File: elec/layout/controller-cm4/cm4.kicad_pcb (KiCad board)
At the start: 2 copper layers, 15 parts, among them U10 12.4kΩ ±1% 62.5mW, U13 1MΩ ±1% 62.5mW, U32 49.9Ω ±1% 62.5mW, U37 10kΩ ±1% 62.5mW

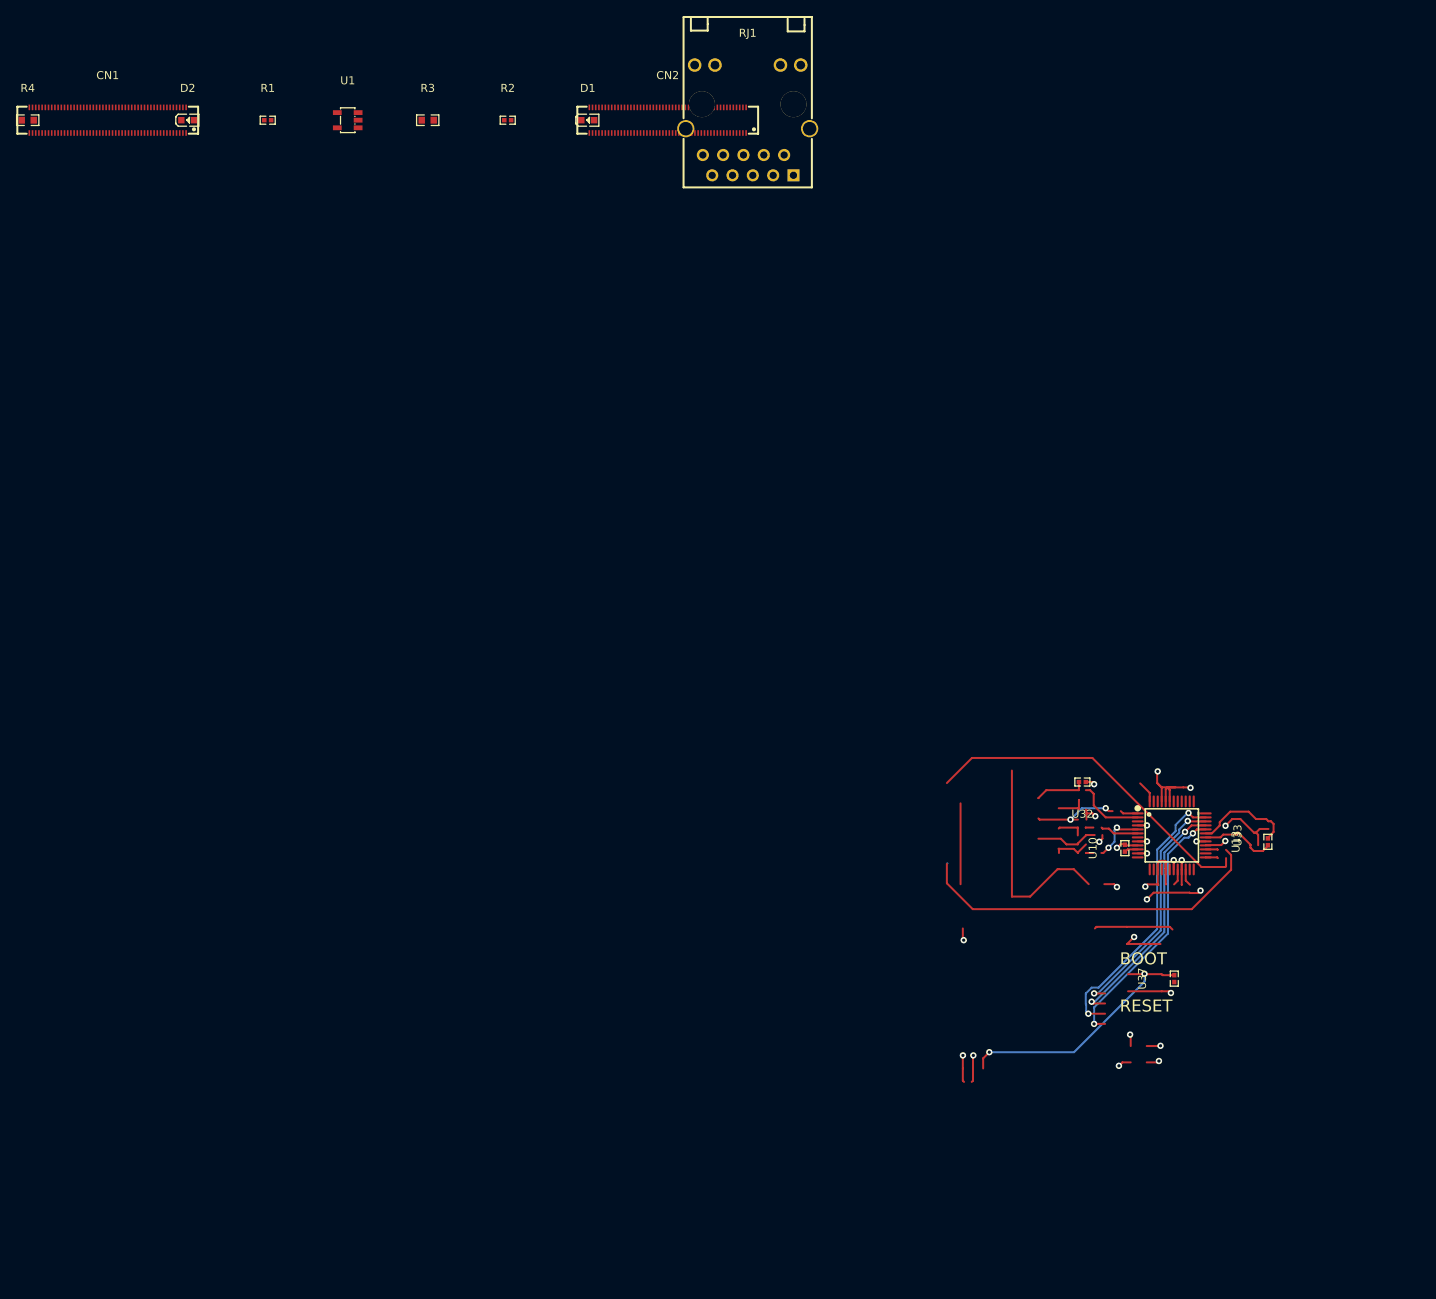
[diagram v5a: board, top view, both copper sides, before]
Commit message: Fix layout for CM4, update ato, delete CM4 example, replacing with SpaceBMSHIL
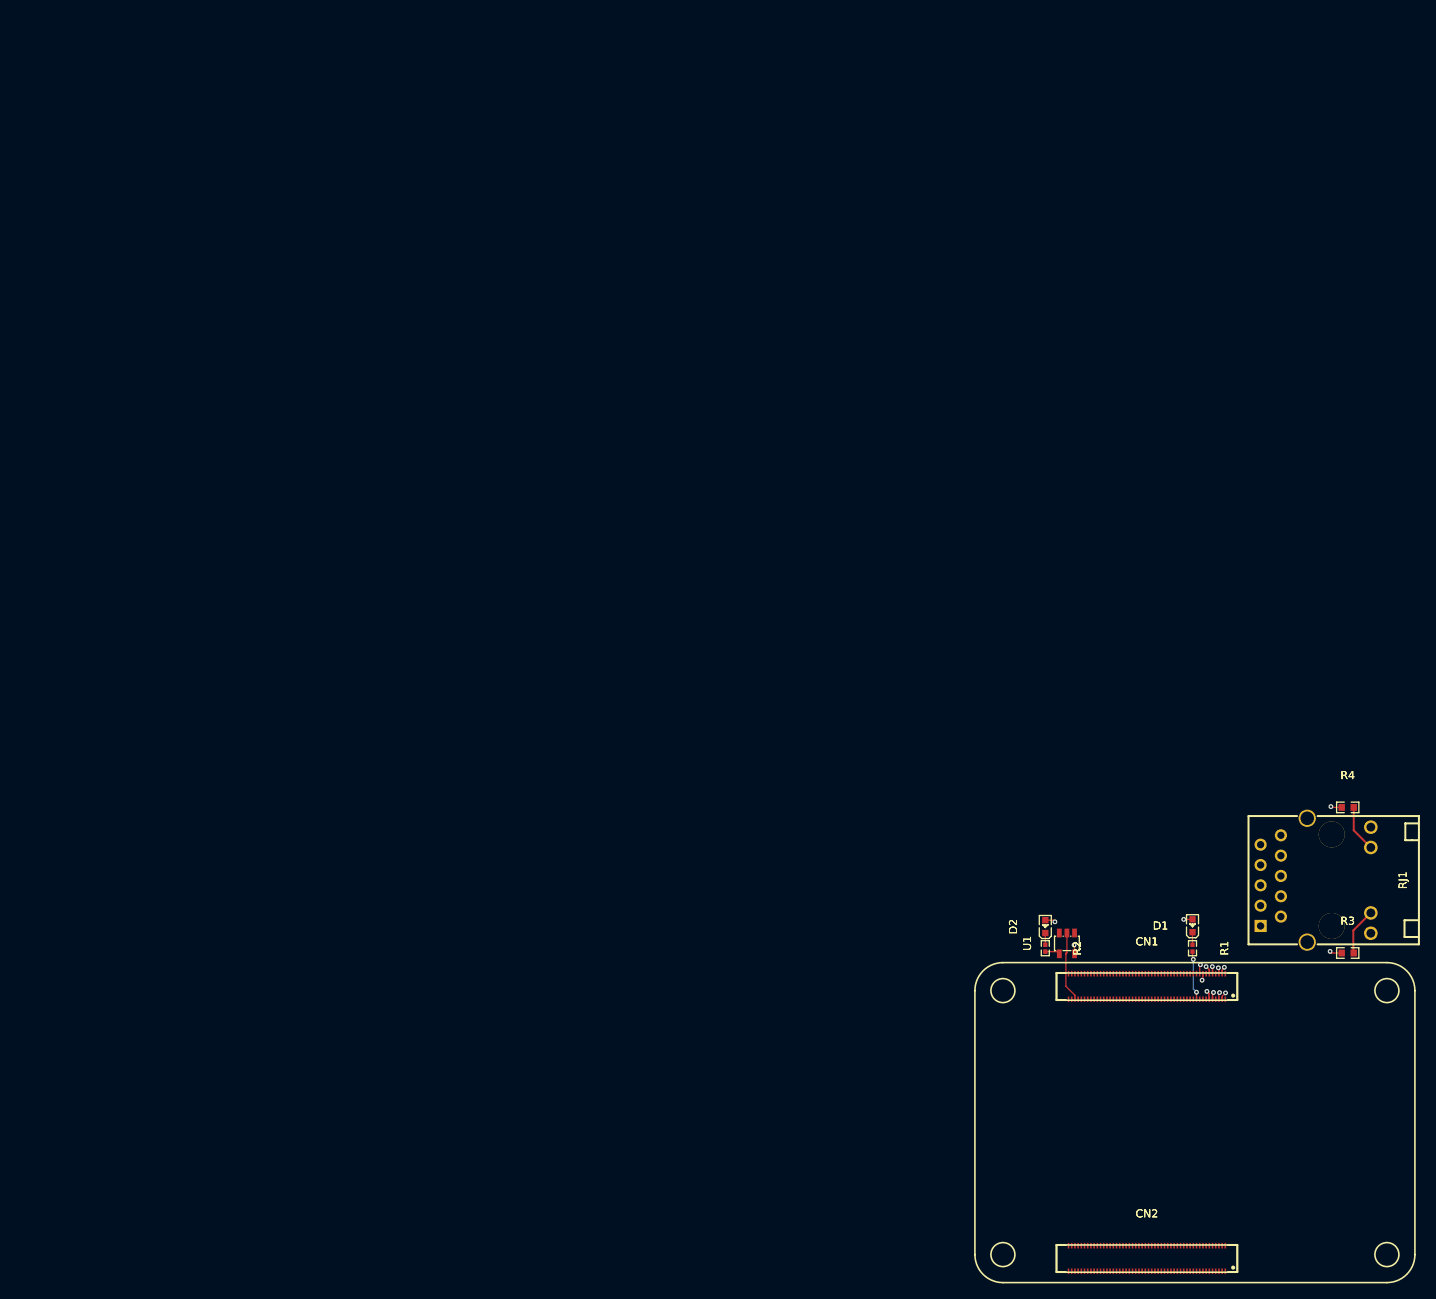
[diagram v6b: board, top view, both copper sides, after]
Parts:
- removed U10: 12.4kΩ ±1% 62.5mW, atopile:R0402-56259e
- removed U13: 1MΩ ±1% 62.5mW, atopile:R0402-56259e
- removed U32: 49.9Ω ±1% 62.5mW, atopile:R0402-56259e
- removed U33: , lib:LQFP-48_L7.0-W7.0-P0.50-LS9.0-BL
- removed U37: 10kΩ ±1% 62.5mW, atopile:R0402-56259e
- moved R4 186.0 mm to (175.0, 80.9)
- moved CN1 169.1 mm to (149.9, 103.3)
- moved R1 155.2 mm to (155.6, 98.5), turned to -90 degrees
- moved R3 155.1 mm to (175.0, 99.1)
- moved CN2 154.4 mm to (149.9, 137.3)
- moved D2 147.1 mm to (137.2, 95.8), turned to 90 degrees
- moved U1 136.6 mm to (139.9, 97.9), turned to 90 degrees
- moved D1 125.9 mm to (155.6, 95.7), turned to 90 degrees
- moved R2 123.4 mm to (137.2, 98.5), turned to -90 degrees
- moved RJ1 118.6 mm to (171.0, 90.0), turned to -90 degrees
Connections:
- net cm4-pins[44]-1 renamed pins[44]
- net cm4.hdi_b-pins[23] renamed pins[23]
- net cm4.hdi_b-pins[28] renamed pins[28]
- net cm4.hdi_b-pins[40] renamed pins[40]
- net cm4.hdi_b-pins[49] renamed pins[49]
- net pins[26] renamed cm4.hdi_b-pins[26]
- net pins[38] renamed cm4.hdi_b-pins[38]
- net pins[39] renamed cm4.hdi_b-pins[39]
- CN1 pad 12: cm4-pins[23] -> cm4-line-4
- CN1 pad 17: line-1 -> line-2
- CN1 pad 20: cm4-line-4 -> cm4-pins[39]
- CN1 pad 22: cm4-line-3 -> pins[43]
- CN1 pad 25: cm4-pins[49] -> cm4-line-5
- CN1 pad 27: line-2 -> line-1
- CN1 pad 28: cm4-line-7 -> pins[55]
- CN1 pad 29: pins[57] -> cm4-line-3
- CN1 pad 78: cm4-pins[44] -> cm4-line-1
- CN1 pad 80: cm4-pins[40] -> cm4-line-7
- CN1 pad 81: cm4-line-6 -> cm4-pins[38]
- CN1 pad 85: cm4-line-1 -> pins[30]
- CN1 pad 86: cm4-pins[28] -> cm4-line-6
- CN1 pad 87: cm4-line-5 -> cm4-pins[26]
- D1 pad 1: cm4-cathode -> cm4-cathode-1
- D2 pad 1: cm4-cathode-1 -> cm4-cathode
- R1 pad 1: cm4-cathode -> cm4-cathode-1
- R2 pad 1: cm4-cathode-1 -> cm4-cathode
- R3 pad 2: rj45-anode-1 -> rj45-anode
- R4 pad 2: rj45-anode -> rj45-anode-1
- RJ1 pad 12: rj45-anode-1 -> rj45-anode
- RJ1 pad 13: rj45-anode -> rj45-anode-1
- RJ1 pad P1: rj45.connector-net -> rj45.connector-net-1
- RJ1 pad P10: rj45.connector-net-1 -> rj45.connector-net
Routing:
- net (no net): track 460.3 -> 6.43 mm, vias 39 -> 5
- net ETH_LED_ACTIVITY: track 0.00 -> 32.0 mm, vias 0 -> 1
- net ETH_LED_LINK: track 0.00 -> 27.0 mm, vias 0 -> 1
- net ETH_P0_N: track 0.00 -> 21.0 mm, vias 0 -> 1
- net ETH_P3_P: track 0.00 -> 19.4 mm, vias 0 -> 1
- net ETH_P1_N: track 0.00 -> 19.2 mm, vias 0 -> 1
- net ETH_P3_N: track 0.00 -> 18.3 mm, vias 0 -> 1
- net ETH_P0_P: track 0.00 -> 18.0 mm, vias 0 -> 1
- net ETH_P1_P: track 0.00 -> 17.6 mm, vias 0 -> 1
- net ETH_P2_N: track 0.00 -> 16.1 mm, vias 0 -> 1
- net ETH_P2_P: track 0.00 -> 14.7 mm, vias 0 -> 1
- net PWR_LED: track 0.00 -> 8.93 mm
- net RXN: track 6.82 -> 0.00 mm, vias 2 -> 0
- net TD_plus: track 6.51 -> 0.00 mm
- net pins[19]: track 0.00 -> 6.16 mm, vias 0 -> 2
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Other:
- copper layers 2 -> 4
- board text removed: "BOOT"
- board text removed: "RESET"

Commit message: Everything builds
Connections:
- net cm4-pins[39] renamed cm4-line-8
- net cm4.hdi_b-pins[26] renamed pins[26]
- net cm4.hdi_b-pins[39] renamed pins[39]
- net pins[23] renamed cm4.hdi_b-pins[23]
- net pins[28] renamed cm4.hdi_b-pins[28]
- net pins[40] renamed cm4.hdi_b-pins[40]
- net pins[44] renamed cm4-pins[44]-1
- CN1 pad 12: cm4-line-4 -> cm4-pins[23]
- CN1 pad 15: line -> line-1
- CN1 pad 17: line-2 -> line-3
- CN1 pad 19: pins[37] -> cm4-line-6
- CN1 pad 23: pins[45] -> cm4-line-2
- CN1 pad 25: cm4-line-5 -> cm4-line-4
- CN1 pad 27: line-1 -> line-2
- CN1 pad 75: cm4-line-2 -> pins[50]
- CN1 pad 78: cm4-line-1 -> cm4-pins[44]
- CN1 pad 80: cm4-line-7 -> cm4-pins[40]
- CN1 pad 82: line-3 -> line
- CN1 pad 85: pins[30] -> cm4-line-7
- CN1 pad 86: cm4-line-6 -> cm4-pins[28]
- CN1 pad 87: cm4-pins[26] -> cm4-line-1
- R2 pad 2: Y -> cm4-line-5
- R3 pad 2: rj45-anode -> rj45-anode-1
- R4 pad 2: rj45-anode-1 -> rj45-anode
- RJ1 pad 12: rj45-anode -> rj45-anode-1
- RJ1 pad 13: rj45-anode-1 -> rj45-anode
- RJ1 pad P1: rj45.connector-net-1 -> rj45.connector-net
- RJ1 pad P10: rj45.connector-net -> rj45.connector-net-1
- U1 pad 4: Y -> cm4-line-5
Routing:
- net cm4-line-5: track 0.00 -> 1.86 mm
- net Y: track 1.86 -> 0.00 mm

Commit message: Cleanup
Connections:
- CN1 pad 1: (no net) -> GND
- CN1 pad 100: (no net) -> GND
- CN1 pad 11: (no net) -> GND
- CN1 pad 16: (no net) -> GND
- CN1 pad 21: (no net) -> GND
- CN1 pad 26: (no net) -> GND
- CN1 pad 30: (no net) -> GND
- CN1 pad 33: (no net) -> GND
- CN1 pad 37: (no net) -> GND
- CN1 pad 4: (no net) -> GND
- CN1 pad 49: (no net) -> GND
- CN1 pad 65: (no net) -> GND
- CN1 pad 68: (no net) -> GND
- CN1 pad 7: (no net) -> GND
- CN1 pad 71: (no net) -> GND
- CN1 pad 74: (no net) -> GND
- CN1 pad 79: (no net) -> GND
- CN1 pad 84: (no net) -> GND
- CN1 pad 89: (no net) -> GND
- CN1 pad 90: (no net) -> GND
- CN1 pad 94: (no net) -> GND
- CN1 pad 97: (no net) -> GND
- CN2 pad 10: (no net) -> GND
- CN2 pad 13: (no net) -> GND
- CN2 pad 16: (no net) -> GND
- CN2 pad 19: (no net) -> GND
- CN2 pad 22: (no net) -> GND
- CN2 pad 28: (no net) -> GND
- CN2 pad 31: (no net) -> GND
- CN2 pad 34: (no net) -> GND
- CN2 pad 37: (no net) -> GND
- CN2 pad 4: (no net) -> GND
- CN2 pad 40: (no net) -> GND
- CN2 pad 43: (no net) -> GND
- CN2 pad 46: (no net) -> GND
- CN2 pad 49: (no net) -> GND
- CN2 pad 52: (no net) -> GND
- CN2 pad 55: (no net) -> GND
- CN2 pad 58: (no net) -> GND
- CN2 pad 61: (no net) -> GND
- CN2 pad 64: (no net) -> GND
- CN2 pad 67: (no net) -> GND
- CN2 pad 7: (no net) -> GND
- CN2 pad 70: (no net) -> GND
- CN2 pad 73: (no net) -> GND
- CN2 pad 82: (no net) -> GND
- CN2 pad 85: (no net) -> GND
- CN2 pad 88: (no net) -> GND
- CN2 pad 91: (no net) -> GND
- CN2 pad 94: (no net) -> GND
- CN2 pad 97: (no net) -> GND
- U1 pad 3: GND -> (no net)
